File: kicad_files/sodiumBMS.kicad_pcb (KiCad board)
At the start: 0 parts

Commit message: added symbols for TPS and INA2, sim values for TPS
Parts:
- added Q1: AO3400A, Package_TO_SOT_SMD:SOT-23, F.Cu at (121.9, 98.5)
- added Q3: AO3400A, Package_TO_SOT_SMD:SOT-23, F.Cu at (159.0, 100.4)
- added U1: STM32F446RETx, Package_QFP:LQFP-64_10x10mm_P0.5mm, F.Cu at (142.8, 88.2)
- added U2: INA180A4, Package_TO_SOT_SMD:SOT-23-5, F.Cu at (154.0, 100.4)
- added U3: INA180A4, Package_TO_SOT_SMD:SOT-23-5, F.Cu at (154.0, 104.8)
- added U4: LM3940, Package_TO_SOT_SMD:SOT-89-3, F.Cu at (131.0, 89.5)
- added U5: TPS61088RHLR, footprints:RHL0020A, F.Cu at (131.0, 98.8)
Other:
- copper layers 0 -> 2

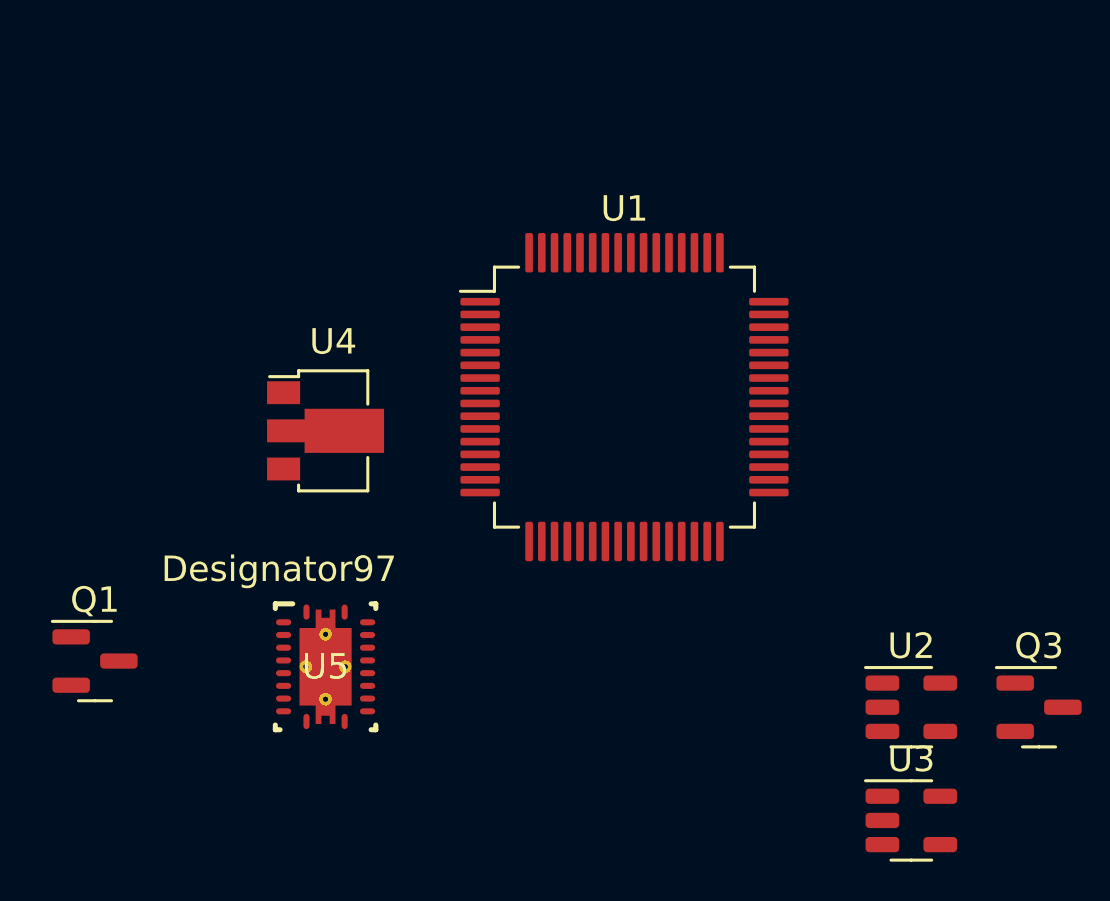
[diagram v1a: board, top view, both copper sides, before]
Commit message: trying to add ina2180 footprint and symbol but didn't succed on footprint
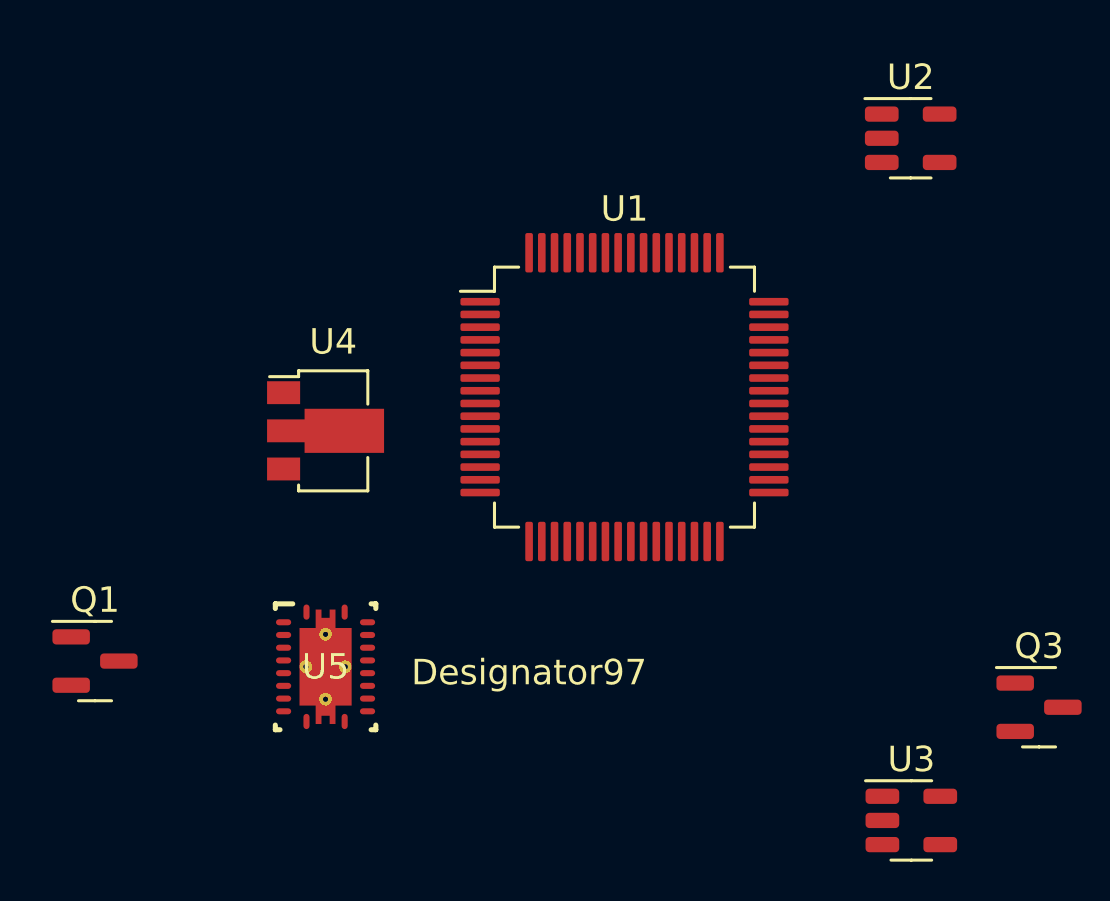
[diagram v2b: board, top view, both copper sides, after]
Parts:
- moved U2 22.4 mm to (154.0, 78.0)
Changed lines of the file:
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@@
 	(footprint "Package_TO_SOT_SMD:SOT-23-5"
 		(layer "F.Cu")
-		(at 154.025 100.365)
+		(at 154 78)
 		(descr "SOT, 5 Pin (https://www.jedec.org/sites/default/files/docs/Mo-178c.PDF variant AA), generated with kicad-footprint-generator ipc_gullwing_generator.py")
 		(tags "SOT TO_SOT_SMD")
@@
 		)
 		(property "Value" "TPS61088RHLR"
-			(at 0 0 0)
+			(at 0 3.724999 0)
 			(unlocked yes)
 			(layer "F.Fab")
@@
 		)
 		(fp_text user "Designator97"
-			(at -1.8288 -3.8354 0)
+			(at 8 0.224999 0)
 			(unlocked yes)
 			(layer "F.SilkS")

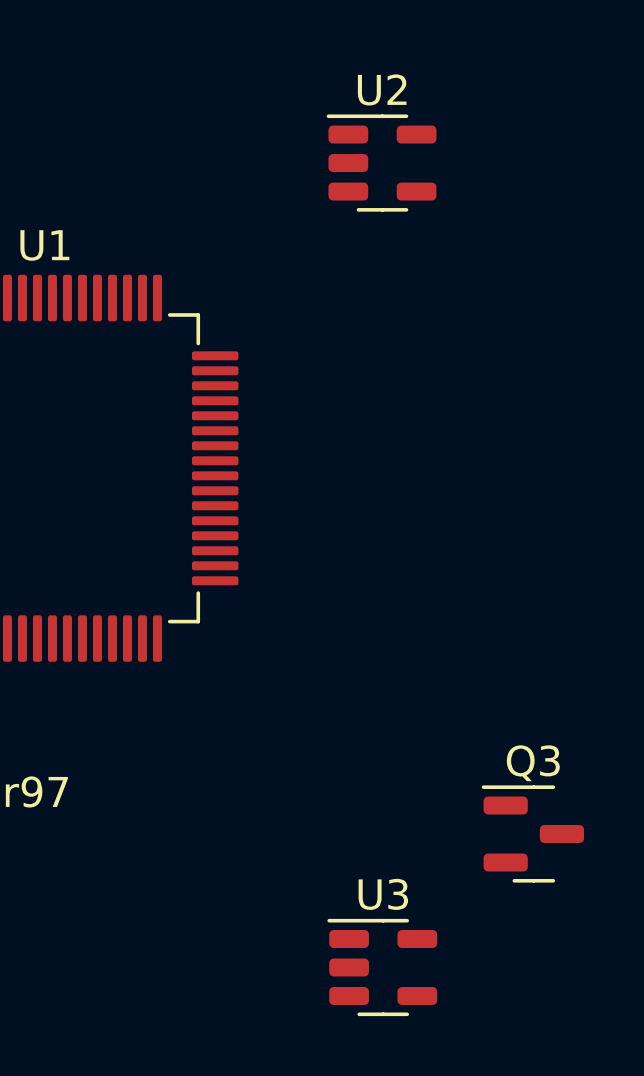
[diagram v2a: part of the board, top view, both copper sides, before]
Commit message: got footprint for current sense amp working
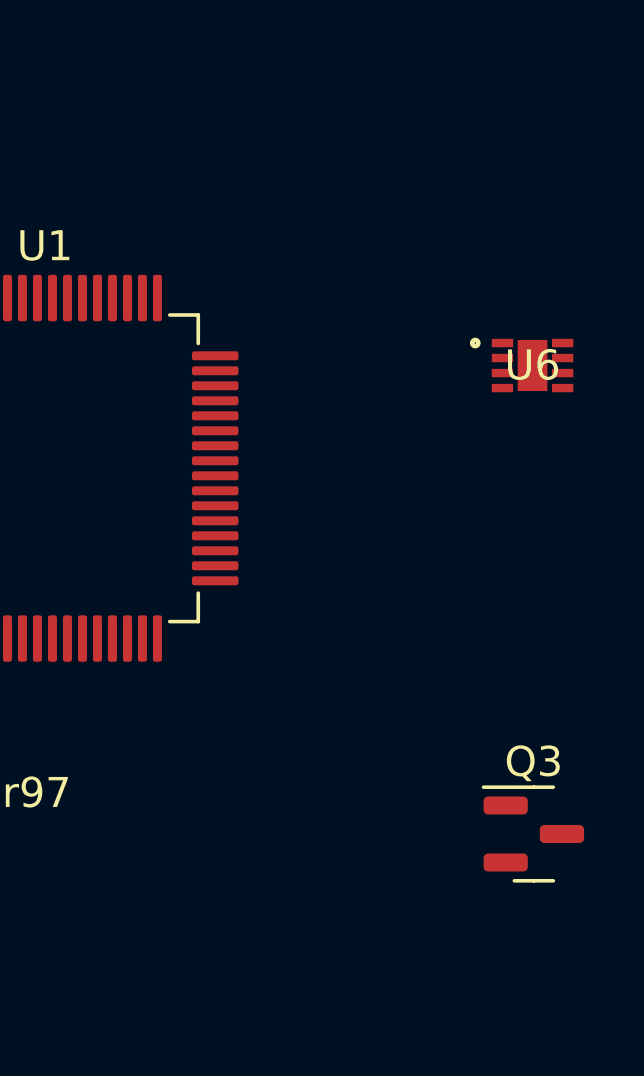
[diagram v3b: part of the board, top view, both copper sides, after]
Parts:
- removed U2, U3: INA180A4, Package_TO_SOT_SMD:SOT-23-5
- added U6: INA2180A4, sodiumBMS_extras:WSON8_DSG_TEX, F.Cu at (159.0, 84.8)

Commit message: more laying out
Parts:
- added C1: 1.5nF ish, Capacitor_SMD:C_0805_2012Metric_Pad1.18x1.45mm_HandSolder, F.Cu at (219.8, 95.1)
- added C10: 8.2nF, Capacitor_SMD:C_0805_2012Metric_Pad1.18x1.45mm_HandSolder, F.Cu at (152.0, 119.5)
- added C11: 856.774pF, Capacitor_SMD:C_0805_2012Metric_Pad1.18x1.45mm_HandSolder, F.Cu at (152.0, 122.5)
- added C12: 40.732pF, Capacitor_SMD:C_0805_2012Metric_Pad1.18x1.45mm_HandSolder, F.Cu at (152.0, 125.6)
- added C13: 22uF, Capacitor_SMD:C_0805_2012Metric_Pad1.18x1.45mm_HandSolder, F.Cu at (156.8, 110.5)
- added C14: 22uF, Capacitor_SMD:C_0805_2012Metric_Pad1.18x1.45mm_HandSolder, F.Cu at (156.8, 113.5)
- added C15: 100nF, Capacitor_SMD:C_0805_2012Metric_Pad1.18x1.45mm_HandSolder, F.Cu at (156.8, 116.5)
- added C16: 100nF, Capacitor_SMD:C_0805_2012Metric_Pad1.18x1.45mm_HandSolder, F.Cu at (156.8, 119.5)
- added C17: 10uF, Capacitor_SMD:C_0805_2012Metric_Pad1.18x1.45mm_HandSolder, F.Cu at (156.8, 122.5)
- added C2: 1.5nF ish, Capacitor_SMD:C_0805_2012Metric_Pad1.18x1.45mm_HandSolder, F.Cu at (219.8, 98.1)
- added C3: 1.5nF ish, Capacitor_SMD:C_0805_2012Metric_Pad1.18x1.45mm_HandSolder, F.Cu at (219.8, 101.1)
- added C4: 33uF, Capacitor_SMD:C_0805_2012Metric_Pad1.18x1.45mm_HandSolder, F.Cu at (156.7, 130.6)
- added C5: 0.47uF, Capacitor_SMD:C_0805_2012Metric_Pad1.18x1.45mm_HandSolder, F.Cu at (156.7, 133.6)
- added C6: 4.7uF, Capacitor_SMD:C_0805_2012Metric_Pad1.18x1.45mm_HandSolder, F.Cu at (156.7, 136.6)
- added C7: 10uF, Capacitor_SMD:C_0805_2012Metric_Pad1.18x1.45mm_HandSolder, F.Cu at (152.0, 110.5)
- added C8: 1uF, Capacitor_SMD:C_0805_2012Metric_Pad1.18x1.45mm_HandSolder, F.Cu at (152.0, 113.5)
- added C9: 10uF, Capacitor_SMD:C_0805_2012Metric_Pad1.18x1.45mm_HandSolder, F.Cu at (152.0, 116.5)
- added F1: Fuse, Fuse:Fuseholder_Clip-5x20mm_Eaton_1A5601-01_Inline_P20.80x6.76mm_D1.70mm_Horizontal, F.Cu at (204.5, 89.4)
- added L1: 1.4uH, Inductor_SMD:L_0201_0603Metric, F.Cu at (160.4, 124.6)
- added R1: 20k, Resistor_SMD:R_0805_2012Metric_Pad1.20x1.40mm_HandSolder, F.Cu at (166.0, 83.0)
- added R10: 5.1k, Resistor_SMD:R_0805_2012Metric_Pad1.20x1.40mm_HandSolder, F.Cu at (151.9, 133.5)
- added R11: 162k, Resistor_SMD:R_0805_2012Metric_Pad1.20x1.40mm_HandSolder, F.Cu at (161.5, 110.5)
- added R12: 261k, Resistor_SMD:R_0805_2012Metric_Pad1.20x1.40mm_HandSolder, F.Cu at (161.5, 113.4)
- added R13: 20.5k, Resistor_SMD:R_0805_2012Metric_Pad1.20x1.40mm_HandSolder, F.Cu at (161.5, 116.4)
- added R14: 825k, Resistor_SMD:R_0805_2012Metric_Pad1.20x1.40mm_HandSolder, F.Cu at (161.5, 119.3)
- added R15: 92k, Resistor_SMD:R_0805_2012Metric_Pad1.20x1.40mm_HandSolder, F.Cu at (161.5, 122.3)
- added R16: 3.3k, Resistor_SMD:R_0805_2012Metric_Pad1.20x1.40mm_HandSolder, F.Cu at (151.9, 136.4)
- added R17: 30k, Resistor_SMD:R_0805_2012Metric_Pad1.20x1.40mm_HandSolder, F.Cu at (151.9, 139.4)
- added R18: 100k, Resistor_SMD:R_0805_2012Metric_Pad1.20x1.40mm_HandSolder, F.Cu at (151.9, 142.3)
- added R2: 100k, Resistor_SMD:R_0805_2012Metric_Pad1.20x1.40mm_HandSolder, F.Cu at (166.0, 88.0)
- added R3: 40k, Resistor_SMD:R_0805_2012Metric_Pad1.20x1.40mm_HandSolder, F.Cu at (176.0, 83.0)
- added R4: 20k, Resistor_SMD:R_0805_2012Metric_Pad1.20x1.40mm_HandSolder, F.Cu at (176.0, 88.0)
- added R5: 60k, Resistor_SMD:R_0805_2012Metric_Pad1.20x1.40mm_HandSolder, F.Cu at (186.0, 83.0)
- added R6: 20k, Resistor_SMD:R_0805_2012Metric_Pad1.20x1.40mm_HandSolder, F.Cu at (186.0, 88.0)
- added R7: 0.05, Resistor_SMD:R_0805_2012Metric_Pad1.20x1.40mm_HandSolder, F.Cu at (227.0, 91.0)
- added R8: 0.05, Resistor_SMD:R_0805_2012Metric_Pad1.20x1.40mm_HandSolder, F.Cu at (228.0, 73.5)
- added R9: 5.1k, Resistor_SMD:R_0805_2012Metric_Pad1.20x1.40mm_HandSolder, F.Cu at (151.9, 130.5)
- moved Q3 69.7 mm to (227.1, 85.0)
- moved U6 60.5 mm to (219.5, 84.8)
- moved U4 19.5 mm to (142.2, 73.5)
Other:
- board text added: "protection and sensing"
